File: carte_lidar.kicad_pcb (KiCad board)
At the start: 4 copper layers, 68 x 68 mm, 62 parts, among them J1 Conn_01x03_Pin, J10 Conn_01x06_Socket, J11 Conn_01x06_Socket, J12 Conn_01x06_Socket, J2 Conn_01x02_Pin, J3 Conn_01x05_Socket, J4 Conn_01x02, J5 Conn_01x02_Pin, J6 Conn_01x06_Socket, J8 USB_C_Receptacle_USB2.0_16P, J9 Conn_01x06_Socket, SW1 SW_Push, U1 TPS54302, U2 RP2040, U3 W25Q128JVS, U5 USBLC6-2P6, U6 NM/AMS1117-3.3, U7 MPU-6000, X1 S2D12.000000B20F30T

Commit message: update
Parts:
- added C31: 1uF 6.3V, Capacitor_SMD:C_0402_1005Metric, F.Cu at (106.5, 83.0)
- added C32: 1uF 6.3V, Capacitor_SMD:C_0402_1005Metric, F.Cu at (101.2, 83.2)
- added C33: 1uF 6.3V, Capacitor_SMD:C_0402_1005Metric, F.Cu at (100.3, 95.0)
- added C34: 1uF 6.3V, Capacitor_SMD:C_0402_1005Metric, F.Cu at (107.2, 94.2)
- added C35: 1uF 6.3V, Capacitor_SMD:C_0402_1005Metric, F.Cu at (97.8, 87.4)
- added C36: 1uF 6.3V, Capacitor_SMD:C_0402_1005Metric, F.Cu at (110.0, 88.8)
- added F1: JK-SMD300L-24V, Fuse:Fuse_2920_7451Metric, F.Cu at (70.7, 104.1)
- added J13: Conn_01x02, Connector_JST:JST_XH_B2B-XH-AM_1x02_P2.50mm_Vertical, F.Cu at (77.3, 116.3)
- added JP1: SolderJumper_2_Open, Jumper:SolderJumper-2_P1.3mm_Open_RoundedPad1.0x1.5mm, F.Cu at (129.3, 106.2)
- added JP2: SolderJumper_2_Open, Jumper:SolderJumper-2_P1.3mm_Open_RoundedPad1.0x1.5mm, F.Cu at (84.9, 73.0)
- added U9: NM/AMS1117-3.3, Package_TO_SOT_SMD:SOT-223-3_TabPin2, F.Cu at (81.6, 78.9)
- C26: value 1uF 10V -> 1uF 6.3V
- R17: value 5.1k -> 10k
- U2: footprint Package_DFN_QFN:QFN-56-1EP_7x7mm_P0.4mm_EP3.2x3.2mm_ThermalVias -> Package_DFN_QFN:QFN-56-1EP_7x7mm_P0.4mm_EP3.2x3.2mm
- moved R15 11.7 mm to (82.3, 84.8), turned to 90 degrees
- moved J4 9.47 mm to (99.9, 72.0)
- moved J5 9.24 mm to (108.2, 72.0), turned to 90 degrees
- moved LED2 9.17 mm to (79.8, 84.8), turned to 0 degrees
- moved J1 8.60 mm to (90.6, 76.2)
- moved R18 7.24 mm to (72.0, 113.4), turned to 90 degrees
- moved R17 6.09 mm to (71.0, 111.4)
- moved C22 5.80 mm to (70.9, 113.4), turned to -90 degrees
- moved R5 5.20 mm to (94.9, 76.8), turned to -90 degrees
- moved J2 4.66 mm to (71.0, 91.0)
- moved C3 4.46 mm to (74.0, 110.0), turned to 0 degrees
- moved R8 3.02 mm to (126.9, 91.1), turned to 90 degrees
- moved C25 2.13 mm to (110.8, 86.9)
- moved R13 1.87 mm to (109.1, 90.2), turned to 180 degrees
- moved R4 1.34 mm to (96.8, 73.7)
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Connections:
- C1 pad 1: /power/VBAT -> /power/VBAT_FUZED
- C2 pad 1: /power/VBAT -> /power/VBAT_FUZED
- C3 pad 1: /power/VBAT -> /power/VBAT_FUZED
- R17 pad 2: /power/VBAT -> /power/VBAT_FUZED
- U1 pad 3: /power/VBAT -> /power/VBAT_FUZED
- U6 pad 2: +3V3 -> Net-(JP1-A)
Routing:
- net /power/VBAT: track 27.3 -> 4.44 mm
- net scl: track 59.1 -> 81.5 mm
- net sda: track 67.1 -> 88.5 mm
- net GND: track 58.7 -> 75.1 mm, vias 19 -> 35
- net +5V: track 25.3 -> 38.6 mm
- net +3V3: track 46.0 -> 57.8 mm, vias 22 -> 25
- net Net-(JP2-A): track 0.00 -> 11.3 mm
- net /power/VBAT_FUZED: track 0.00 -> 10.0 mm
- net Net-(JP1-A): track 0.00 -> 8.53 mm
- net /+1.1V: track 12.6 -> 18.6 mm
- net BAT_SENSE: track 50.2 -> 46.8 mm
- net tof1: track 81.0 -> 84.2 mm
- net Net-(J1-Pin_3): track 8.69 -> 5.64 mm
- net /motoct: track 15.4 -> 17.9 mm
- net /led: track 12.7 -> 10.3 mm
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- added copper zone on F.Cu, net /power/VBAT_FUZED
- removed copper zone on F.Cu, net /power/VBAT
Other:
- board text added: "3.3V"
- board text added: "I2C"
- board text added: "mpu-6000"
- board text added: "slc"

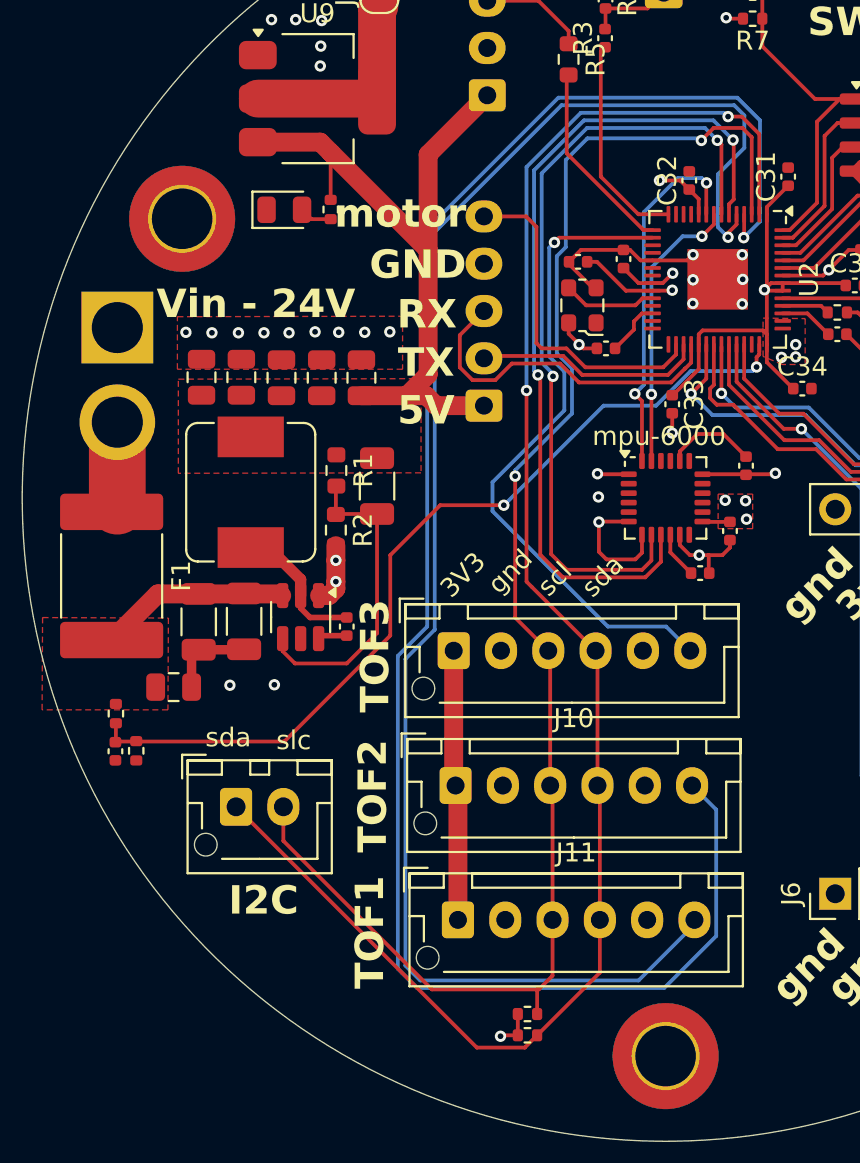
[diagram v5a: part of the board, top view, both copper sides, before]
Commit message: update silkscreen layer
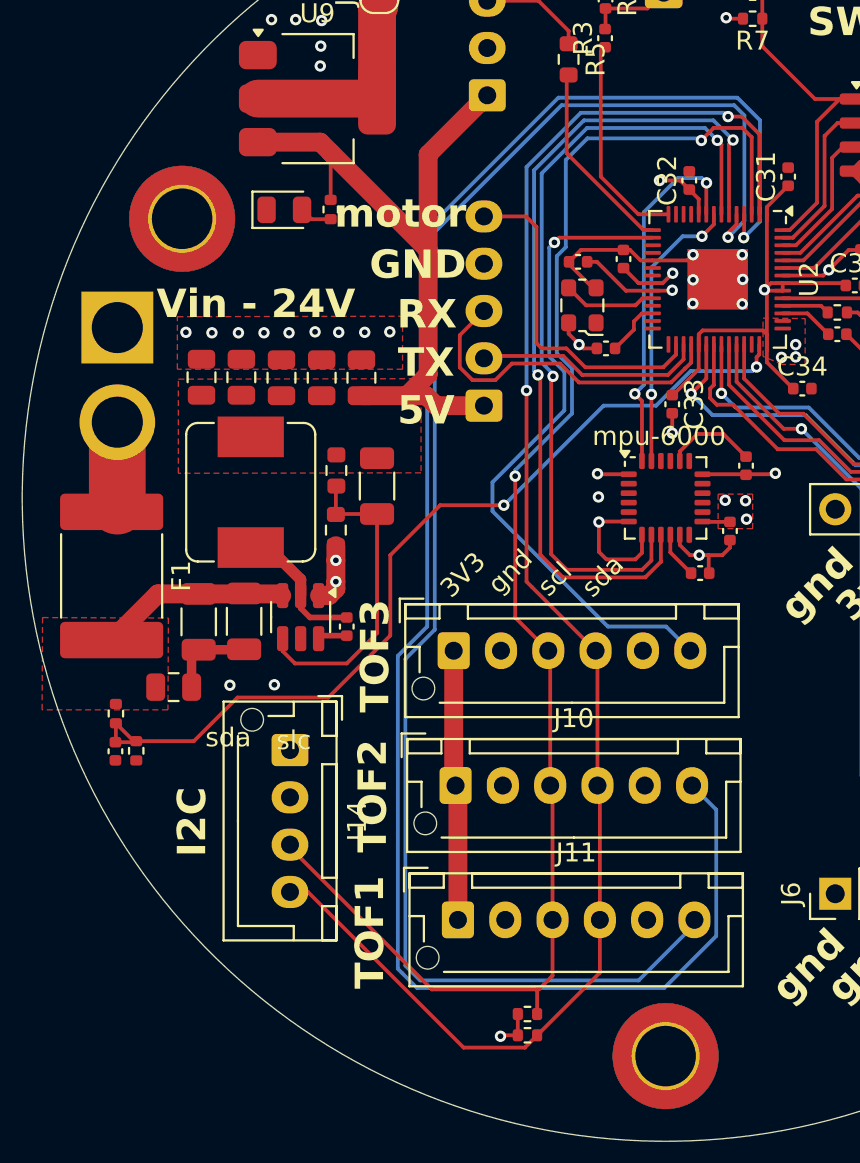
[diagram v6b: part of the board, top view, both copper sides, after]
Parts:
- removed J13: Conn_01x02, Connector_JST:JST_XH_B2B-XH-AM_1x02_P2.50mm_Vertical
- added J14: Conn_01x04_Socket, Connector_JST:JST_XH_B4B-XH-AM_1x04_P2.50mm_Vertical, F.Cu at (80.2, 113.3)
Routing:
- net sda: track 88.5 -> 83.8 mm
- net scl: track 81.5 -> 79.3 mm
- net BAT_SENSE: track 46.8 -> 48.3 mm
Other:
- board text added: "SCL"
- board text added: "SDA"
